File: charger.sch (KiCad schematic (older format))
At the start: 41 parts

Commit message: routing completed
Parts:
- gave numbers to parts that had none: 41

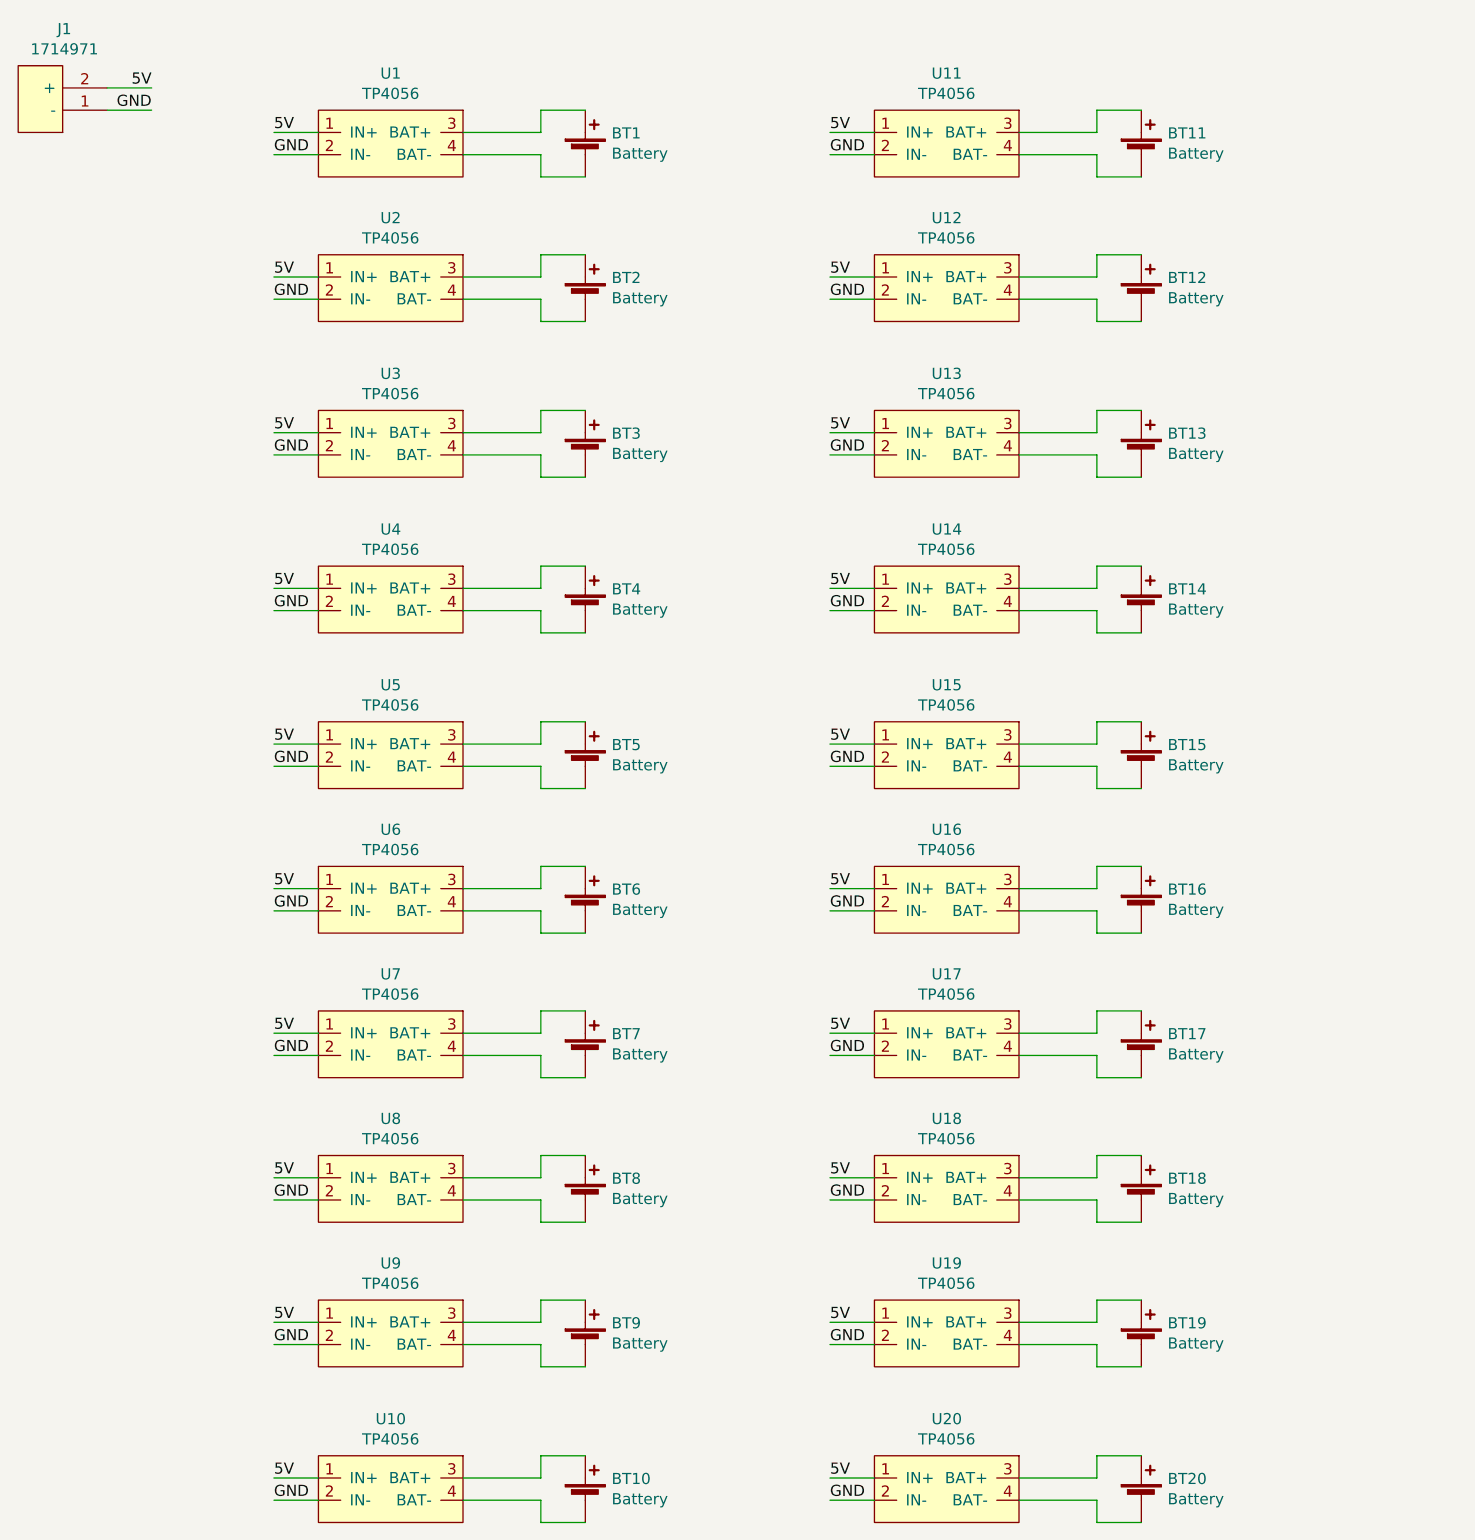
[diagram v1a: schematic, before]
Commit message: added mounting holes
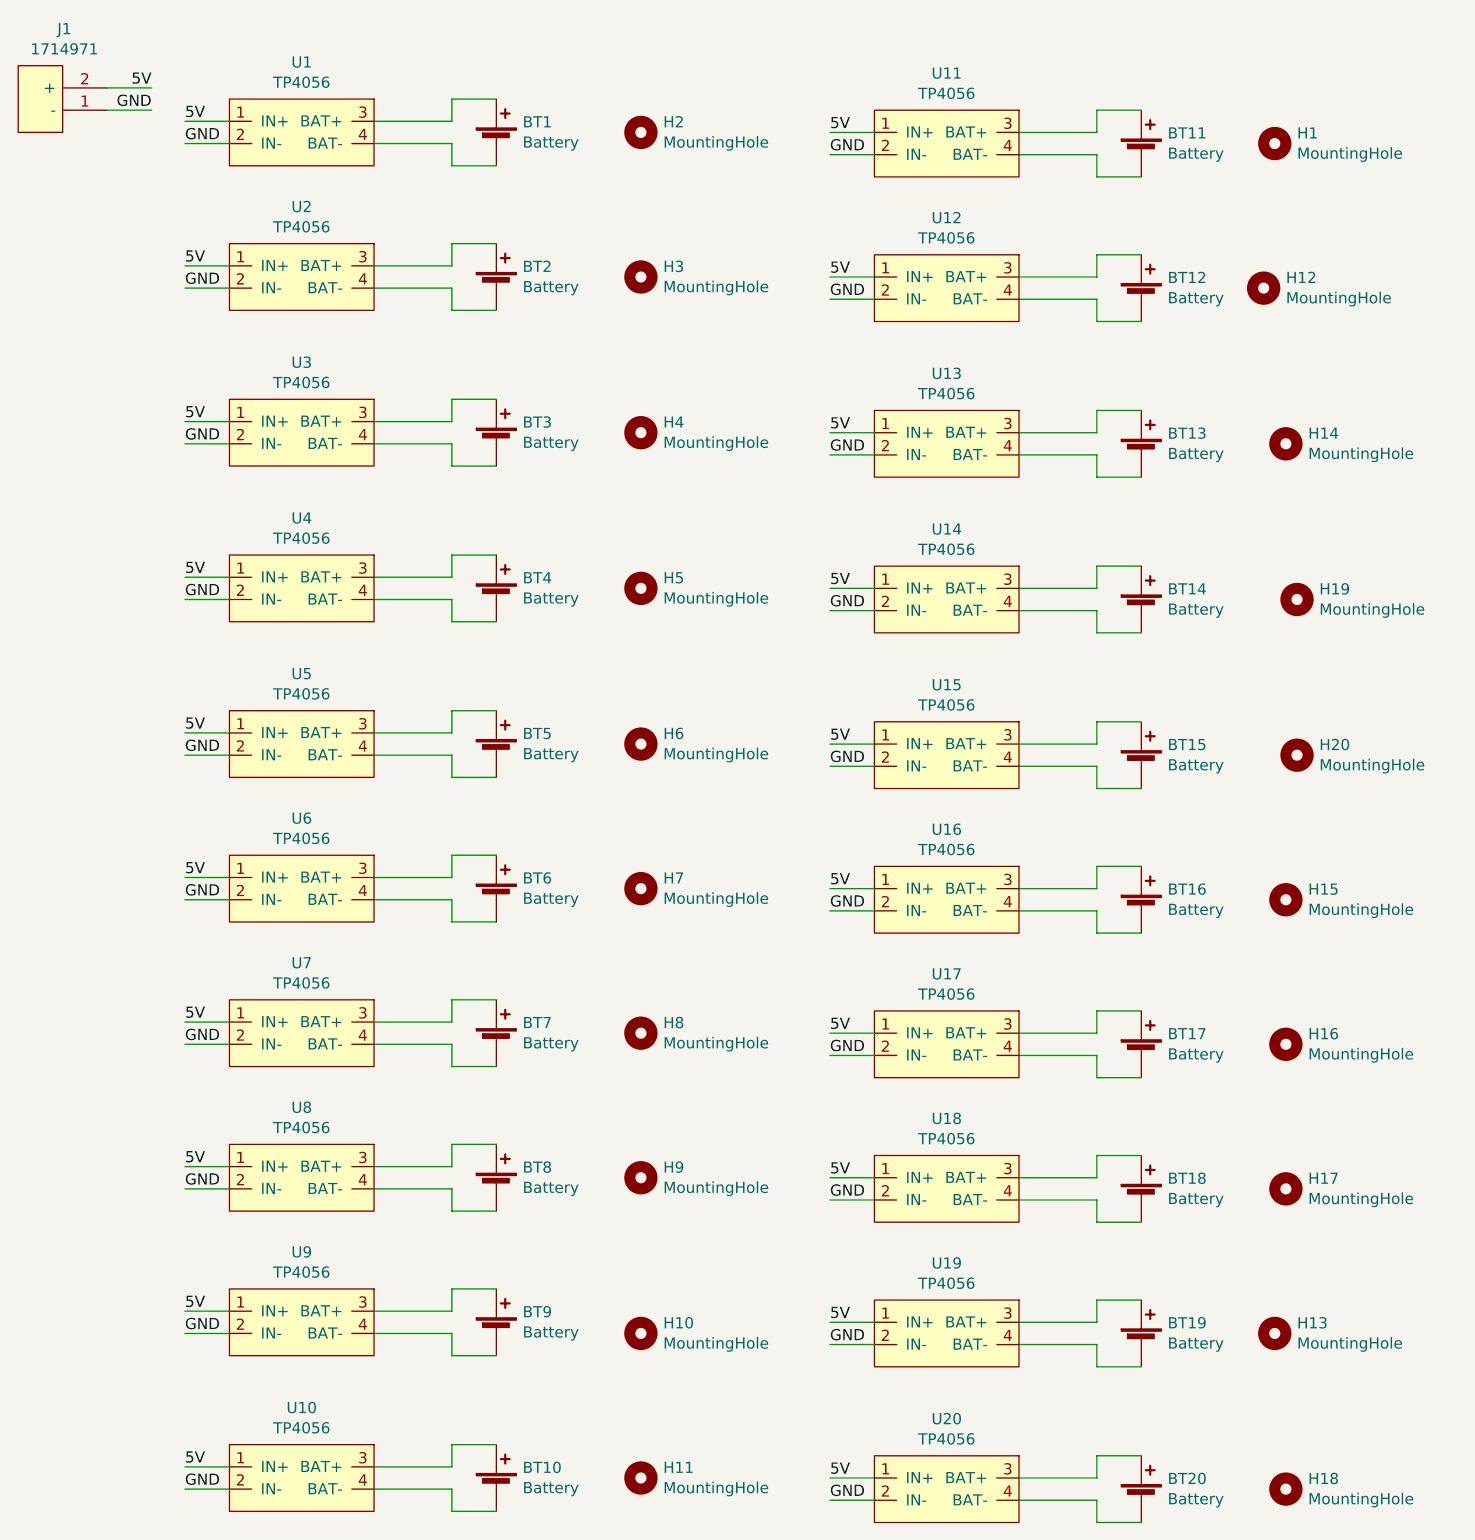
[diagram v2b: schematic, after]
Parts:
- added H1, H10, H11, H12, H13, H14, H15, H16, H17, H18, H19, H2, H20, H3, H4, H5, H6, H7, H8, H9: MountingHole, MountingHole:MountingHole_2.7mm_M2.5, symbol Mechanical:MountingHole
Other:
- moved on the sheet: BT1, BT10, BT2, BT3, BT4, BT5, BT6, BT7, BT8, BT9, U1, U10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

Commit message: added filed zones
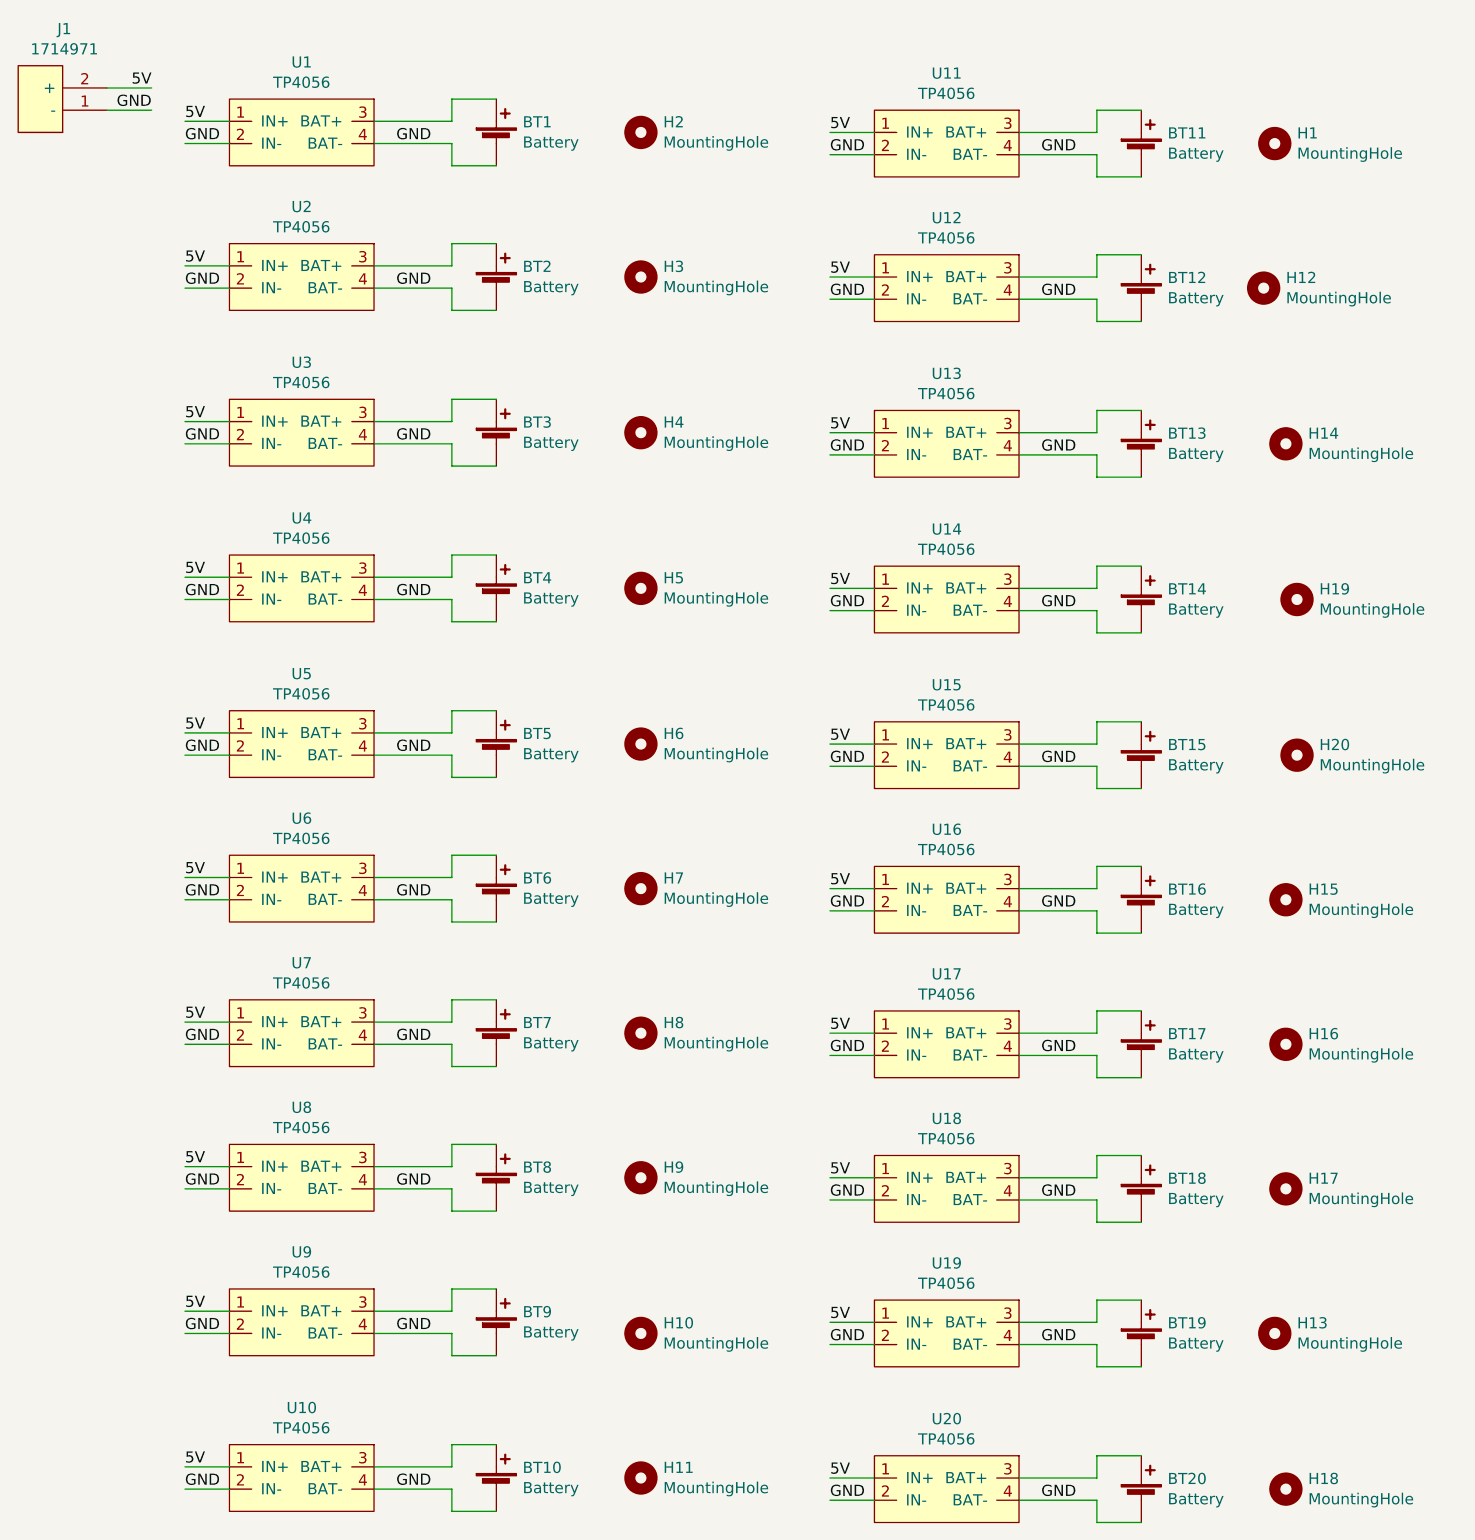
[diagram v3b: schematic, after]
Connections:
- net GND: now also BT1.2 (-), BT10.2 (-), BT11.2 (-), BT12.2 (-), BT13.2 (-), BT14.2 (-), BT15.2 (-), BT16.2 (-), BT17.2 (-), BT18.2 (-), BT19.2 (-), BT2.2 (-), BT20.2 (-), BT3.2 (-), BT4.2 (-), BT5.2 (-), BT6.2 (-), BT7.2 (-), BT8.2 (-), BT9.2 (-), U1.4 (BAT-), U10.4 (BAT-), U11.4 (BAT-), U12.4 (BAT-), U13.4 (BAT-), U14.4 (BAT-), U15.4 (BAT-), U16.4 (BAT-), U17.4 (BAT-), U18.4 (BAT-), U19.4 (BAT-), U2.4 (BAT-), U20.4 (BAT-), U3.4 (BAT-), U4.4 (BAT-), U5.4 (BAT-), U6.4 (BAT-), U7.4 (BAT-), U8.4 (BAT-), U9.4 (BAT-)
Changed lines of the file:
@@
 	1    0    0    -1
 $EndComp
+Text Label 2300 1100 0    50   ~ 0
+GND
+Text Label 2300 1750 0    50   ~ 0
+GND
+Text Label 2300 2450 0    50   ~ 0
+GND
+Text Label 2300 3150 0    50   ~ 0
+GND
+Text Label 2300 3850 0    50   ~ 0
+GND
+Text Label 2300 4500 0    50   ~ 0
+GND
+Text Label 2300 5150 0    50   ~ 0
+GND
+Text Label 2300 5800 0    50   ~ 0
+GND
+Text Label 2300 6450 0    50   ~ 0
+GND
+Text Label 2300 7150 0    50   ~ 0
+GND
+Text Label 5200 7200 0    50   ~ 0
+GND
+Text Label 5200 6500 0    50   ~ 0
+GND
+Text Label 5200 5850 0    50   ~ 0
+GND
+Text Label 5200 5200 0    50   ~ 0
+GND
+Text Label 5200 4550 0    50   ~ 0
+GND
+Text Label 5200 3900 0    50   ~ 0
+GND
+Text Label 5200 3200 0    50   ~ 0
+GND
+Text Label 5200 2500 0    50   ~ 0
+GND
+Text Label 5200 1800 0    50   ~ 0
+GND
+Text Label 5200 1150 0    50   ~ 0
+GND
 $EndSCHEMATC
